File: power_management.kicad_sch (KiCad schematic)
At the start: 22 parts, among them J1 705510001, Q1 SSM3J327R, U6 TLV840MADL22DBVR, U7 TPS22917DBV, U8 OPA333 or TLV333 or TLV9041

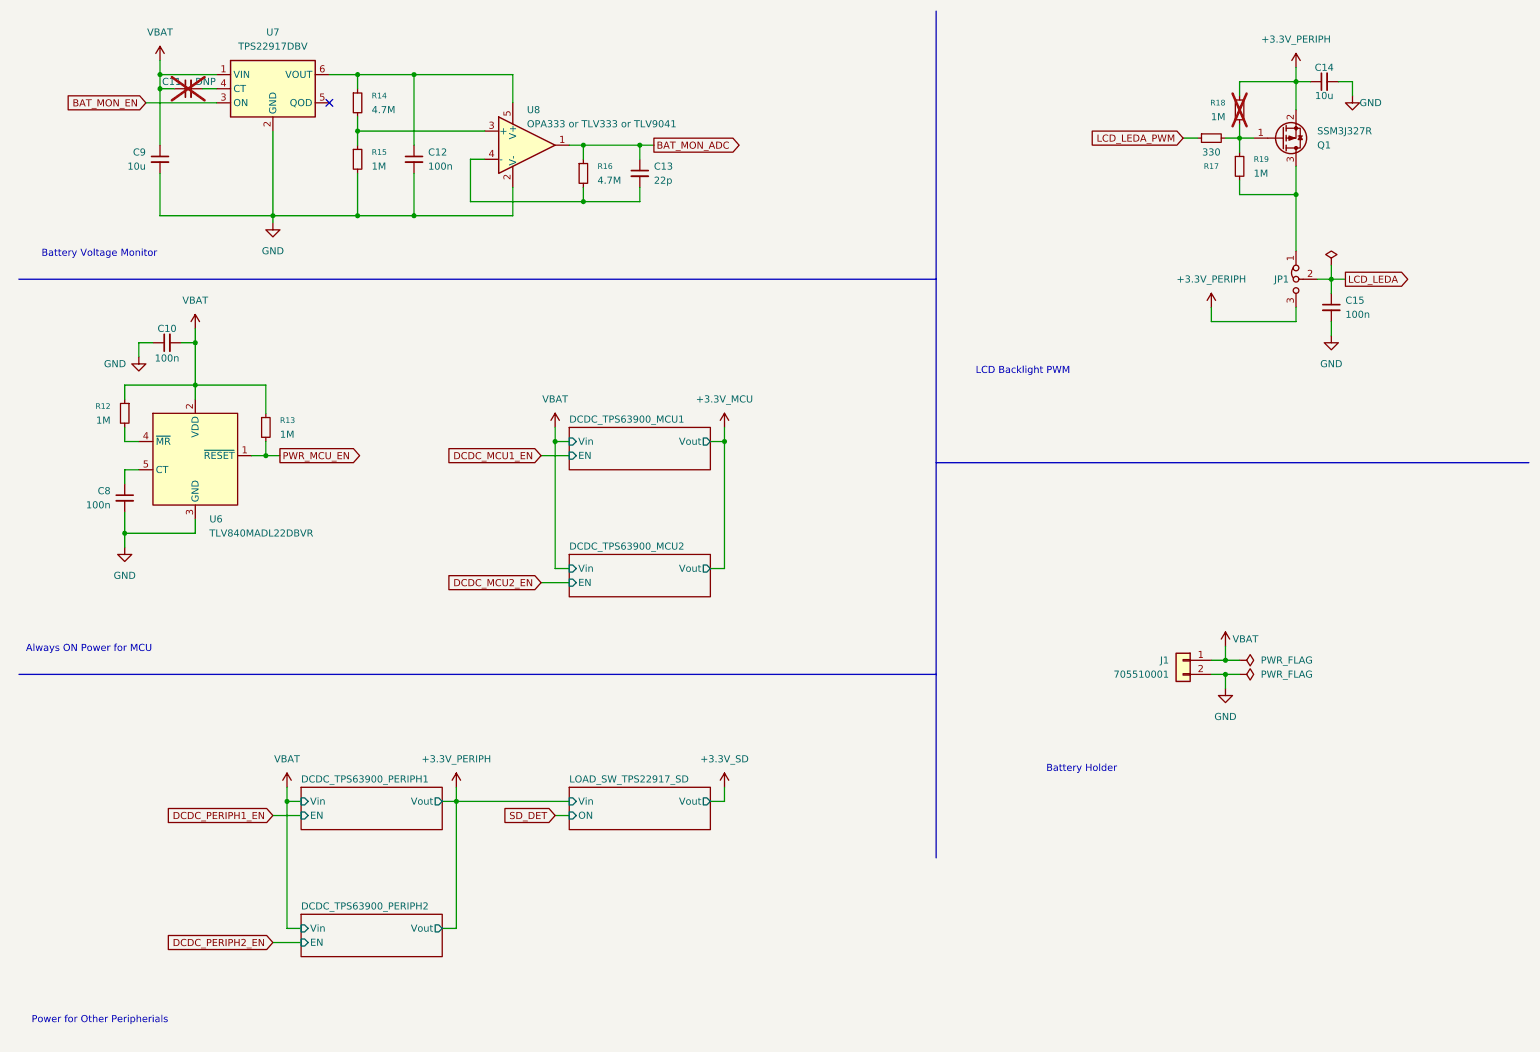
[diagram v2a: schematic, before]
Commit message: Revision to fix problems from first board fab
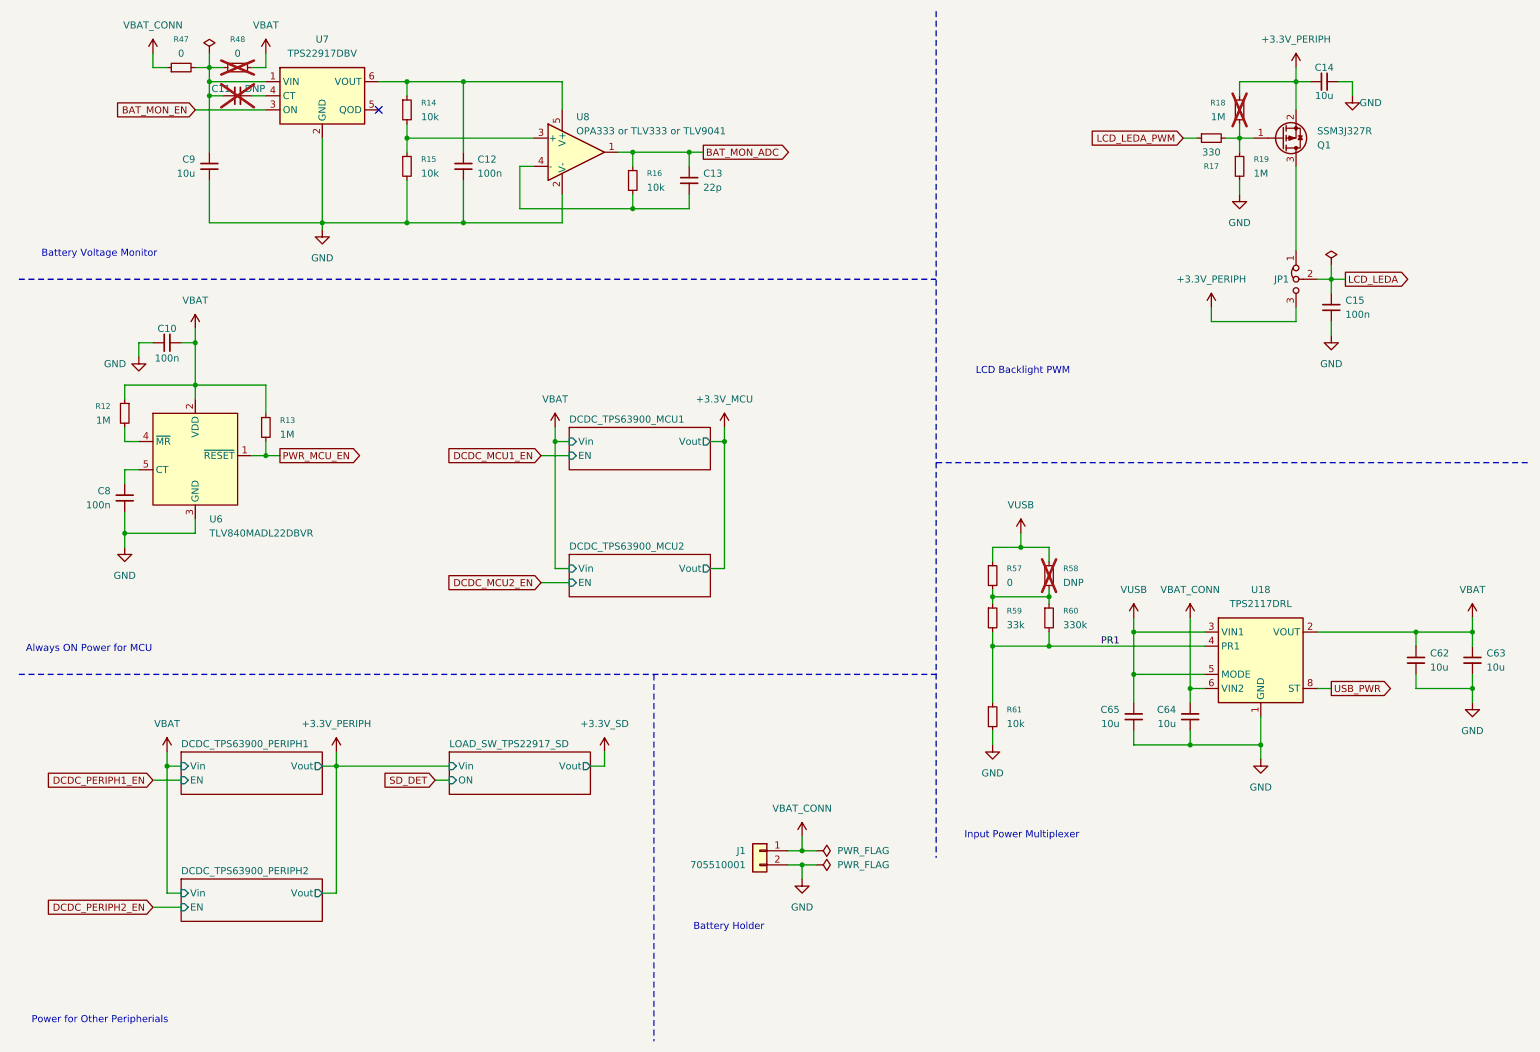
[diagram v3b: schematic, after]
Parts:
- added C62, C63, C64, C65: 10u, Capacitor_SMD:C_0603_1608Metric_Pad1.08x0.95mm_HandSolder, symbol Device:C_Small
- added R47, R48, R57: 0, Resistor_SMD:R_0603_1608Metric_Pad0.98x0.95mm_HandSolder, symbol Device:R_Small
- added R58: DNP, Resistor_SMD:R_0603_1608Metric_Pad0.98x0.95mm_HandSolder, symbol Device:R_Small
- added R59: 33k, Resistor_SMD:R_0603_1608Metric_Pad0.98x0.95mm_HandSolder, symbol Device:R_Small
- added R60: 330k, Resistor_SMD:R_0603_1608Metric_Pad0.98x0.95mm_HandSolder, symbol Device:R_Small
- added R61: 10k, Resistor_SMD:R_0603_1608Metric_Pad0.98x0.95mm_HandSolder, symbol Device:R_Small
- added U18: TPS2117DRL, Package_TO_SOT_SMD:SOT-583-8, symbol Power_Management:TPS2116DRL
- R14, R16: value 4.7M -> 10k
- R15: value 1M -> 10k
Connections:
- net GND: now also R19.2, C62.2, C63.2, C64.2, C65.2, R61.2, U18.1 (GND)
- net VBAT: now also C62.1, C63.1, R48.2, U18.2 (VOUT), U18.7 (VOUT); no longer C11.1, C9.1, J1.1 (Pin_1), U7.1 (VIN)
- net at JP1.1 (A), Q1.3 (D): no longer R19.2
- new net: C11.1, C9.1, R47.2, R48.1, U7.1 (VIN)
- new net: R57.2, R58.2, R59.1, R60.1
- new net PR1: R59.2, R60.2, R61.1, U18.4 (PR1)
- new net USB_PWR: U18.8 (ST)
- new net VBAT_CONN: C64.1, J1.1 (Pin_1), R47.1, U18.6 (VIN2)
- new net VUSB: C65.1, R57.1, R58.1, U18.3 (VIN1), U18.5 (MODE)
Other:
- note added: "Input Power Multiplexer"
- moved on the sheet: C11, C12, C13, C9, J1, R14, R15, R16, U7, U8

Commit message: Final version sent for fabrication
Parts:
- added JP3: Jumper_3_Bridged12, Connector_PinHeader_2.54mm:PinHeader_1x03_P2.54mm_Vertical, symbol Jumper:Jumper_3_Bridged12
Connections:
- net VBAT: now also JP3.2 (C)
- net VBAT_CONN: now also JP3.3 (B)
- net VUSB: now also JP3.1 (A)
